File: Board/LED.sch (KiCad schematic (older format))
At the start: 8 parts, among them Q10 IRLML6344TRPBF

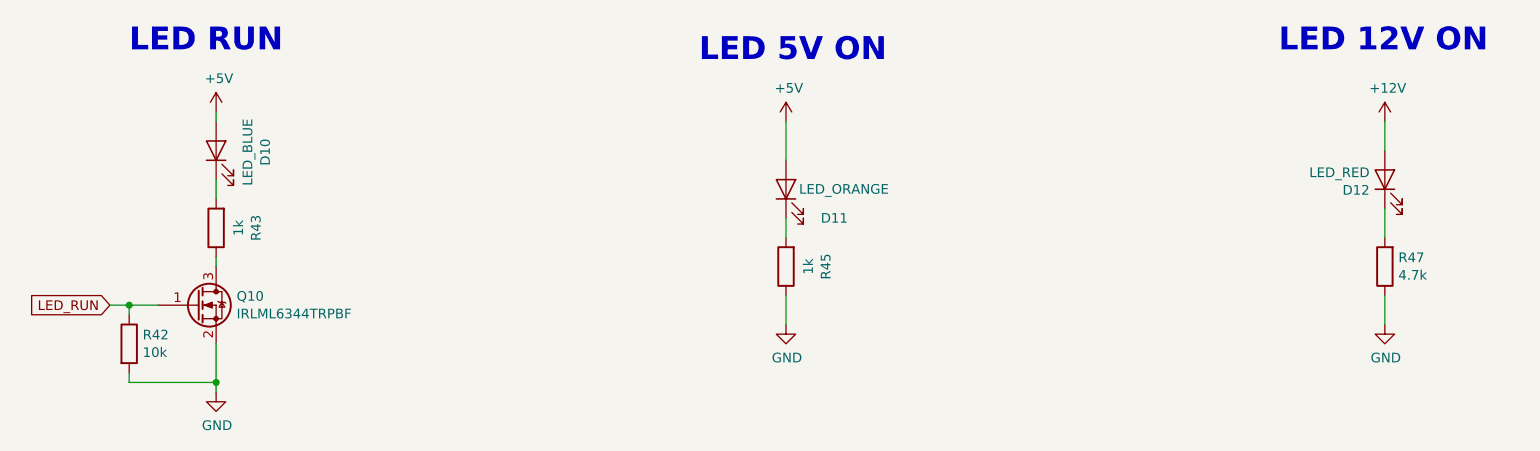
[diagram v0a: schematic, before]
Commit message: Added protection resistors on xmega GPIOs. Corrected prog connector outline.
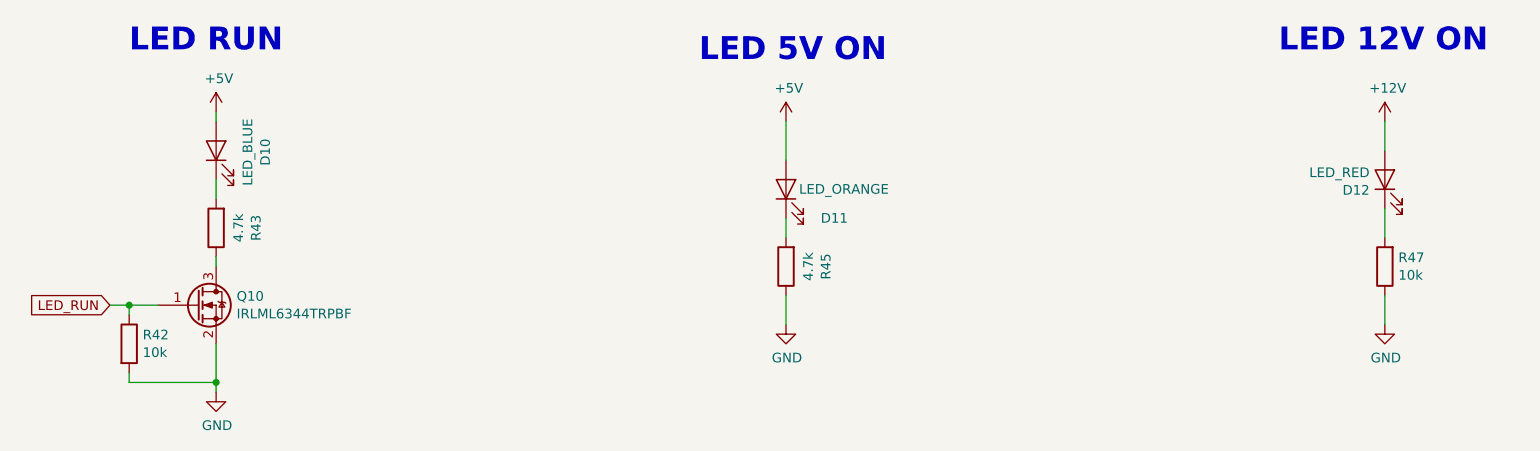
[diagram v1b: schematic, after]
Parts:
- R43, R45: value 1k -> 4.7k
- R47: value 4.7k -> 10k
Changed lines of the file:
@@
 P 2850 3750
 F 0 "R43" V 2643 3750 50  0000 C CNN
-F 1 "1k" V 2734 3750 50  0000 C CNN
+F 1 "4.7k" V 2734 3750 50  0000 C CNN
 F 2 "Resistor_SMD:R_0603_1608Metric_Pad1.05x0.95mm_HandSolder" V 2780 3750 50  0001 C CNN
 F 3 "~" H 2850 3750 50  0001 C CNN
@@
 P 5800 3950
 F 0 "R45" V 5593 3950 50  0000 C CNN
-F 1 "1k" V 5684 3950 50  0000 C CNN
+F 1 "4.7k" V 5684 3950 50  0000 C CNN
 F 2 "Resistor_SMD:R_0603_1608Metric_Pad1.05x0.95mm_HandSolder" V 5730 3950 50  0001 C CNN
 F 3 "~" H 5800 3950 50  0001 C CNN
@@
 P 8900 3950
 F 0 "R47" H 8830 3904 50  0000 R CNN
-F 1 "4.7k" H 8830 3995 50  0000 R CNN
+F 1 "10k" H 8830 3995 50  0000 R CNN
 F 2 "Resistor_SMD:R_0603_1608Metric_Pad1.05x0.95mm_HandSolder" V 8830 3950 50  0001 C CNN
 F 3 "~" H 8900 3950 50  0001 C CNN

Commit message: MAJOR CORRECTION: moved ADCs to correct port on xmega. Added a LED controlled by the xmega.
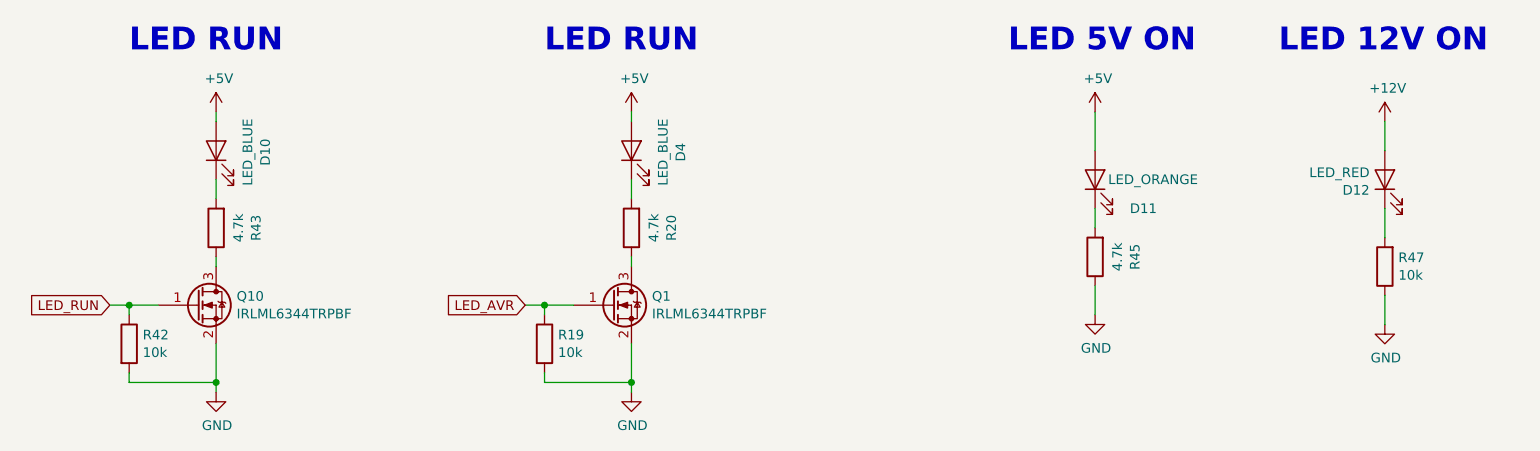
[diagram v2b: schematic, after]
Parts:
- added D4: LED_BLUE, LED_SMD:LED_0603_1608Metric_Pad1.05x0.95mm_HandSolder, symbol Device:LED
- added Q1: IRLML6344TRPBF, Package_TO_SOT_SMD:SOT-23_Handsoldering, symbol Device:Q_NMOS_GSD
- added R19: 10k, Resistor_SMD:R_0603_1608Metric_Pad1.05x0.95mm_HandSolder, symbol Device:R
- added R20: 4.7k, Resistor_SMD:R_0603_1608Metric_Pad1.05x0.95mm_HandSolder, symbol Device:R
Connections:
- net +5V: now also D4.2 (A)
- net GND: now also Q1.2 (S), R19.2
- new net: D4.1 (K), R20.2
- new net: Q1.3 (D), R20.1
- new net LED_AVR: Q1.1 (G), R19.1
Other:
- moved on the sheet: D11, R45
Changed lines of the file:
@@
 L power:GND #PWR?
 U 1 1 5BDD5929
-P 5800 4250
+P 7400 4200
 AR Path="/5BCDDEA9/5BDD5929" Ref="#PWR?"  Part="1"
 AR Path="/5BCDDEAC/5BDD5929" Ref="#PWR039"  Part="1"
-F 0 "#PWR039" H 5800 4000 50  0001 C CNN
-F 1 "GND" H 5805 4077 50  0000 C CNN
-F 2 "" H 5800 4250 50  0001 C CNN
-F 3 "" H 5800 4250 50  0001 C CNN
-	1    5800 4250
+F 0 "#PWR039" H 7400 3950 50  0001 C CNN
+F 1 "GND" H 7405 4027 50  0000 C CNN
+F 2 "" H 7400 4200 50  0001 C CNN
+F 3 "" H 7400 4200 50  0001 C CNN
+	1    7400 4200
 	1    0    0    -1
 $EndComp
@@
 L Device:LED D11
 U 1 1 5BDD5A1E
-P 5800 3550
-F 0 "D11" V 5650 3300 50  0000 C CNN
-F 1 "LED_ORANGE" V 5800 3250 50  0000 C CNN
-F 2 "LED_SMD:LED_0603_1608Metric_Pad1.05x0.95mm_HandSolder" H 5800 3550 50  0001 C CNN
-F 3 "~" H 5800 3550 50  0001 C CNN
-F 4 "2251473" H -3650 2000 50  0001 C CNN "Farnell"
-F 5 "VLMO1300-GS08" H -3650 2000 50  0001 C CNN "Ref"
-	1    5800 3550
+P 7400 3500
+F 0 "D11" V 7250 3250 50  0000 C CNN
+F 1 "LED_ORANGE" V 7400 3200 50  0000 C CNN
+F 2 "LED_SMD:LED_0603_1608Metric_Pad1.05x0.95mm_HandSolder" H 7400 3500 50  0001 C CNN
+F 3 "~" H 7400 3500 50  0001 C CNN
+F 4 "2251473" H -2050 1950 50  0001 C CNN "Farnell"
+F 5 "VLMO1300-GS08" H -2050 1950 50  0001 C CNN "Ref"
+	1    7400 3500
 	0    -1   -1   0
 $EndComp
@@
 L Device:R R45
 U 1 1 5BDD5A25
-P 5800 3950
-F 0 "R45" V 5593 3950 50  0000 C CNN
-F 1 "4.7k" V 5684 3950 50  0000 C CNN
-F 2 "Resistor_SMD:R_0603_1608Metric_Pad1.05x0.95mm_HandSolder" V 5730 3950 50  0001 C CNN
-F 3 "~" H 5800 3950 50  0001 C CNN
-	1    5800 3950
+P 7400 3900
+F 0 "R45" V 7193 3900 50  0000 C CNN
+F 1 "4.7k" V 7284 3900 50  0000 C CNN
+F 2 "Resistor_SMD:R_0603_1608Metric_Pad1.05x0.95mm_HandSolder" V 7330 3900 50  0001 C CNN
+F 3 "~" H 7400 3900 50  0001 C CNN
+	1    7400 3900
 	-1   0    0    1
 $EndComp
@@
 L power:+5V #PWR042
 U 1 1 5BDD5A30
-P 5800 3200
-F 0 "#PWR042" H 5800 3050 50  0001 C CNN
-F 1 "+5V" H 5815 3373 50  0000 C CNN
-F 2 "" H 5800 3200 50  0001 C CNN
-F 3 "" H 5800 3200 50  0001 C CNN
-	1    5800 3200
-	1    0    0    -1
-$EndComp
-Text Notes 5350 2900 0    118  ~ 24
+P 7400 3150
+F 0 "#PWR042" H 7400 3000 50  0001 C CNN
+F 1 "+5V" H 7415 3323 50  0000 C CNN
+F 2 "" H 7400 3150 50  0001 C CNN
+F 3 "" H 7400 3150 50  0001 C CNN
+	1    7400 3150
+	1    0    0    -1
+$EndComp
+Text Notes 6950 2850 0    118  ~ 24
 LED 5V ON
 Text Notes 8350 2850 0    118  ~ 24
@@
 $EndComp
 Wire Wire Line
-	5800 4100 5800 4250
-Wire Wire Line
-	5800 3200 5800 3400
-Wire Wire Line
-	5800 3700 5800 3800
+	7400 4050 7400 4200
+Wire Wire Line
+	7400 3150 7400 3350
+Wire Wire Line
+	7400 3650 7400 3750
+$Comp
+L power:GND #PWR?
+U 1 1 5C14B094
+P 5000 4600
+AR Path="/5BCDDEA9/5C14B094" Ref="#PWR?"  Part="1"
+AR Path="/5BCDDEAC/5C14B094" Ref="#PWR016"  Part="1"
+F 0 "#PWR016" H 5000 4350 50  0001 C CNN
+F 1 "GND" H 5005 4427 50  0000 C CNN
+F 2 "" H 5000 4600 50  0001 C CNN
+F 3 "" H 5000 4600 50  0001 C CNN
+	1    5000 4600
+	1    0    0    -1
+$EndComp
+Wire Wire Line
+	5000 4350 5000 4550
+$Comp
+L Device:R R19
+U 1 1 5C14B09B
+P 4550 4350
+F 0 "R19" H 4620 4396 50  0000 L CNN
+F 1 "10k" H 4620 4305 50  0000 L CNN
+F 2 "Resistor_SMD:R_0603_1608Metric_Pad1.05x0.95mm_HandSolder" V 4480 4350 50  0001 C CNN
+F 3 "~" H 4550 4350 50  0001 C CNN
+	1    4550 4350
+	1    0    0    -1
+$EndComp
+Wire Wire Line
+	4550 4500 4550 4550
+Wire Wire Line
+	4550 4550 5000 4550
+Connection ~ 5000 4550
+Wire Wire Line
+	5000 4550 5000 4600
+Wire Wire Line
+	4550 4200 4550 4150
+Wire Wire Line
+	4550 4150 4700 4150
+Wire Wire Line
+	4550 4150 4450 4150
+Connection ~ 4550 4150
+$Comp
+L Device:LED D4
+U 1 1 5C14B0AC
+P 5000 3350
+F 0 "D4" H 4992 3095 50  0000 C CNN
+F 1 "LED_BLUE" H 4992 3186 50  0000 C CNN
+F 2 "LED_SMD:LED_0603_1608Metric_Pad1.05x0.95mm_HandSolder" H 5000 3350 50  0001 C CNN
+F 3 "~" H 5000 3350 50  0001 C CNN
+F 4 "2251459" H -1050 1700 50  0001 C CNN "Farnell"
+F 5 "VLMB1300-GS08" H -1050 1700 50  0001 C CNN "Ref"
+	1    5000 3350
+	0    -1   -1   0
+$EndComp
+$Comp
+L Device:R R20
+U 1 1 5C14B0B3
+P 5000 3750
+F 0 "R20" V 4793 3750 50  0000 C CNN
+F 1 "4.7k" V 4884 3750 50  0000 C CNN
+F 2 "Resistor_SMD:R_0603_1608Metric_Pad1.05x0.95mm_HandSolder" V 4930 3750 50  0001 C CNN
+F 3 "~" H 5000 3750 50  0001 C CNN
+	1    5000 3750
+	-1   0    0    1
+$EndComp
+Wire Wire Line
+	5000 3600 5000 3500
+Wire Wire Line
+	5000 3200 5000 3150
+Text Notes 4550 2850 0    118  ~ 24
+LED RUN
+Text GLabel 4450 4150 0    50   Input ~ 0
+LED_AVR
+$Comp
+L Device:Q_NMOS_GSD Q1
+U 1 1 5C14B0C0
+P 4900 4150
+F 0 "Q1" H 5106 4196 50  0000 L CNN
+F 1 "IRLML6344TRPBF" H 5106 4105 50  0000 L CNN
+F 2 "Package_TO_SOT_SMD:SOT-23_Handsoldering" H 5100 4250 50  0001 C CNN
+F 3 "~" H 4900 4150 50  0001 C CNN
+F 4 "IRLML6344TRPBF" H 3050 1500 50  0001 C CNN "Farnell"
+F 5 "1857299" H 3050 1500 50  0001 C CNN "Ref"
+	1    4900 4150
+	1    0    0    -1
+$EndComp
+Wire Wire Line
+	5000 3900 5000 3950
+$Comp
+L power:+5V #PWR05
+U 1 1 5C14B0C8
+P 5000 3150
+F 0 "#PWR05" H 5000 3000 50  0001 C CNN
+F 1 "+5V" H 5015 3323 50  0000 C CNN
+F 2 "" H 5000 3150 50  0001 C CNN
+F 3 "" H 5000 3150 50  0001 C CNN
+	1    5000 3150
+	1    0    0    -1
+$EndComp
 $EndSCHEMATC
